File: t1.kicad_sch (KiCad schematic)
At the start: 47 parts, among them J1 Barrel_Jack_Switch, J2 USB_B, J3 P1, J4 2x2M, J5 ICSP1, J6 P2, U1 ATmega8U2-AU, Y1 16MHz

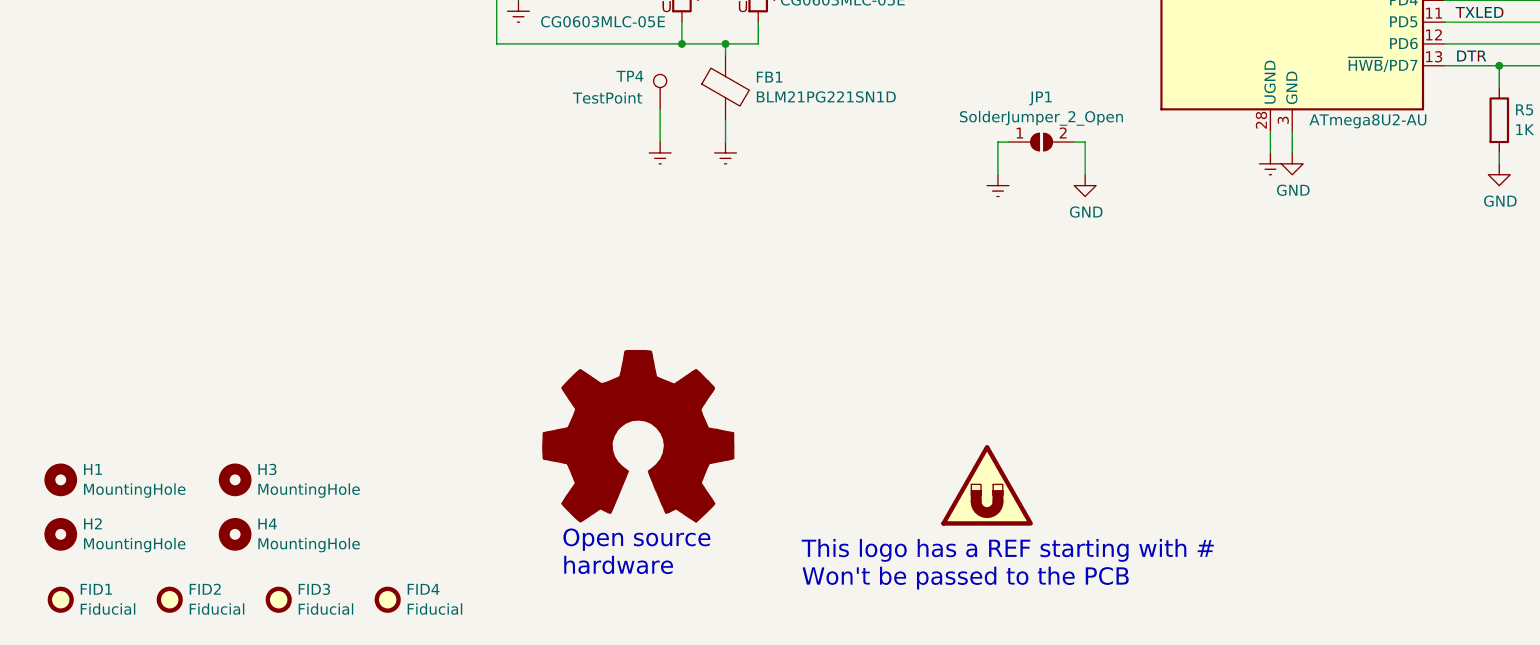
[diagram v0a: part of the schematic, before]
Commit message: More coherence between schematic and PCB
- Same time format, using the generation time stamp
- Same title, adding the variant
- Same worksheet. Why KiCad 6 doesn't respect the first page in the PCB?
- Same revision, short git hash
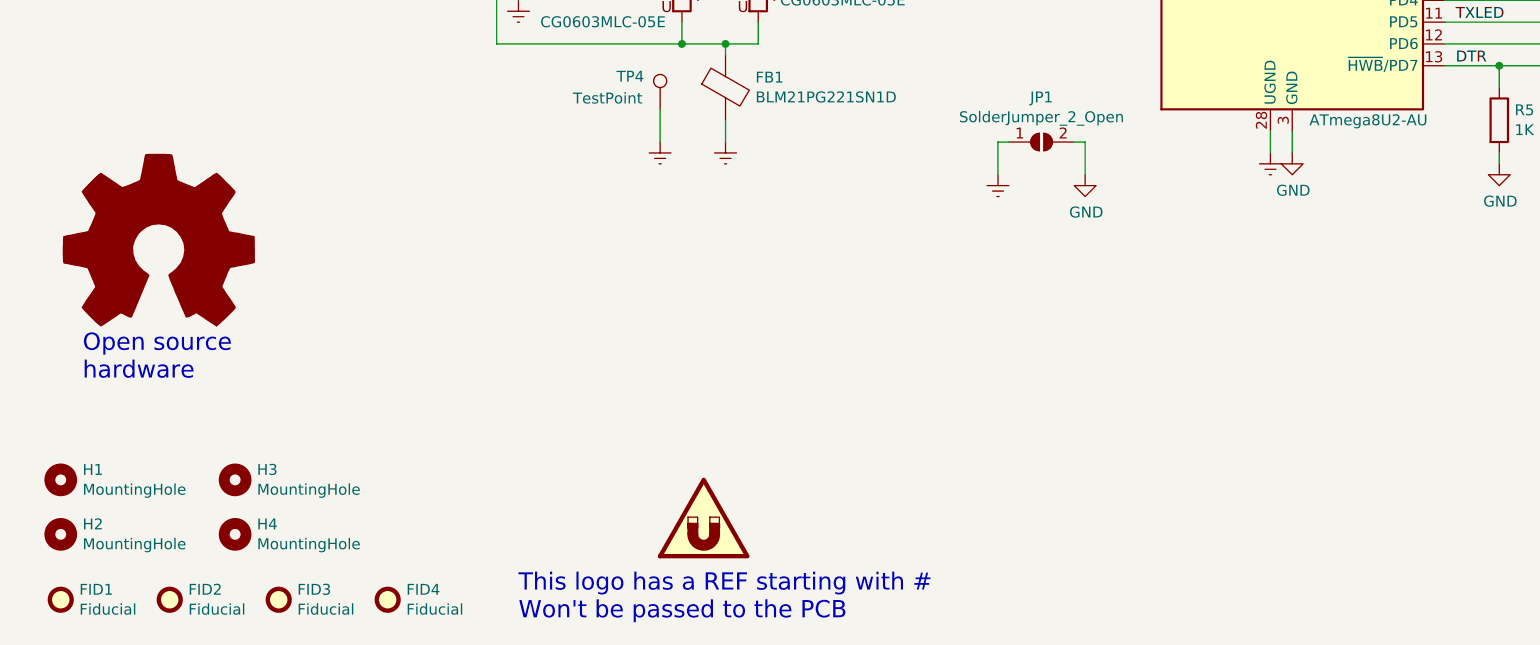
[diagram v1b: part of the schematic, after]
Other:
- company: Arduino -> Instituto Nacional de Tecnología Industrial
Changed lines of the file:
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@@
   (title_block
     (title "Arduino UNO programmer")
-    (date "2020-09-09")
-    (rev "r1")
-    (company "Arduino")
+    (date "${date}")
+    (rev "${git_hash}")
+    (company "Instituto Nacional de Tecnología Industrial")
     (comment 1 "Just a copy of the original circuit, but not as ugly")
+    (comment 4 "An example of KiBot variants")
   )
   (junction (at 82.55 88.9) (diameter 0) (color 0 0 0 0)
@@
     (stroke (width 0) (type default) (color 0 0 0 0))
   )
-  (text "Open source\nhardware" (at 77.47 187.96 0)
+  (text "Open source\nhardware" (at 21.59 165.1 0)
     (effects (font (size 2.0066 2.0066)) (justify left bottom))
   )
   (text "This logo has a REF starting with #\nWon't be passed to the PCB"
-    (at 105.41 189.23 0)
+    (at 72.39 193.04 0)
     (effects (font (size 2.0066 2.0066)) (justify left bottom))
   )
@@
     (pin "1")
   )
-  (symbol (lib_id "Graphic:SYM_Magnet_Large") (at 127 176.53 0) (unit 1)
-    (in_bom yes) (on_board yes)
-    (property "Reference" "#SYM1" (id 0) (at 127 171.45 0)
-      (effects (font (size 1.27 1.27)) hide)
-    )
-    (property "Value" "SYM_Magnet_Large" (id 1) (at 127 182.88 0)
-      (effects (font (size 1.27 1.27)) hide)
-    )
-    (property "Footprint" "" (id 2) (at 127 181.61 0)
-      (effects (font (size 1.27 1.27)) hide)
-    )
-    (property "Datasheet" "~" (id 3) (at 127.762 181.61 0)
+  (symbol (lib_id "Graphic:SYM_Magnet_Large") (at 93.98 180.34 0) (unit 1)
+    (in_bom yes) (on_board yes)
+    (property "Reference" "#SYM1" (id 0) (at 93.98 175.26 0)
+      (effects (font (size 1.27 1.27)) hide)
+    )
+    (property "Value" "SYM_Magnet_Large" (id 1) (at 93.98 186.69 0)
+      (effects (font (size 1.27 1.27)) hide)
+    )
+    (property "Footprint" "" (id 2) (at 93.98 185.42 0)
+      (effects (font (size 1.27 1.27)) hide)
+    )
+    (property "Datasheet" "~" (id 3) (at 94.742 185.42 0)
       (effects (font (size 1.27 1.27)) hide)
     )
@@
     )
   )
-  (symbol (lib_id "Graphic:Logo_Open_Hardware_Large") (at 86.36 172.72 0) (unit 1)
-    (in_bom yes) (on_board yes)
-    (property "Reference" "LOGO1" (id 0) (at 86.36 160.02 0)
-      (effects (font (size 1.27 1.27)) hide)
-    )
-    (property "Value" "Logo_Open_Hardware_Large" (id 1) (at 86.36 182.88 0)
-      (effects (font (size 1.27 1.27)) hide)
-    )
-    (property "Footprint" "Symbol:OSHW-Logo_11.4x12mm_SilkScreen" (id 2) (at 86.36 172.72 0)
-      (effects (font (size 1.27 1.27)) hide)
-    )
-    (property "Datasheet" "~" (id 3) (at 86.36 172.72 0)
-      (effects (font (size 1.27 1.27)) hide)
-    )
+  (symbol (lib_id "Graphic:Logo_Open_Hardware_Large") (at 30.48 149.86 0) (unit 1)
+    (in_bom yes) (on_board yes)
+    (property "Reference" "LOGO1" (id 0) (at 30.48 137.16 0)
+      (effects (font (size 1.27 1.27)) hide)
+    )
+    (property "Value" "Logo_Open_Hardware_Large" (id 1) (at 30.48 160.02 0)
+      (effects (font (size 1.27 1.27)) hide)
+    )
+    (property "Footprint" "Symbol:OSHW-Logo_11.4x12mm_SilkScreen" (id 2) (at 30.48 149.86 0)
+      (effects (font (size 1.27 1.27)) hide)
+    )
+    (property "Datasheet" "~" (id 3) (at 30.48 149.86 0)
+      (effects (font (size 1.27 1.27)) hide)
+    )

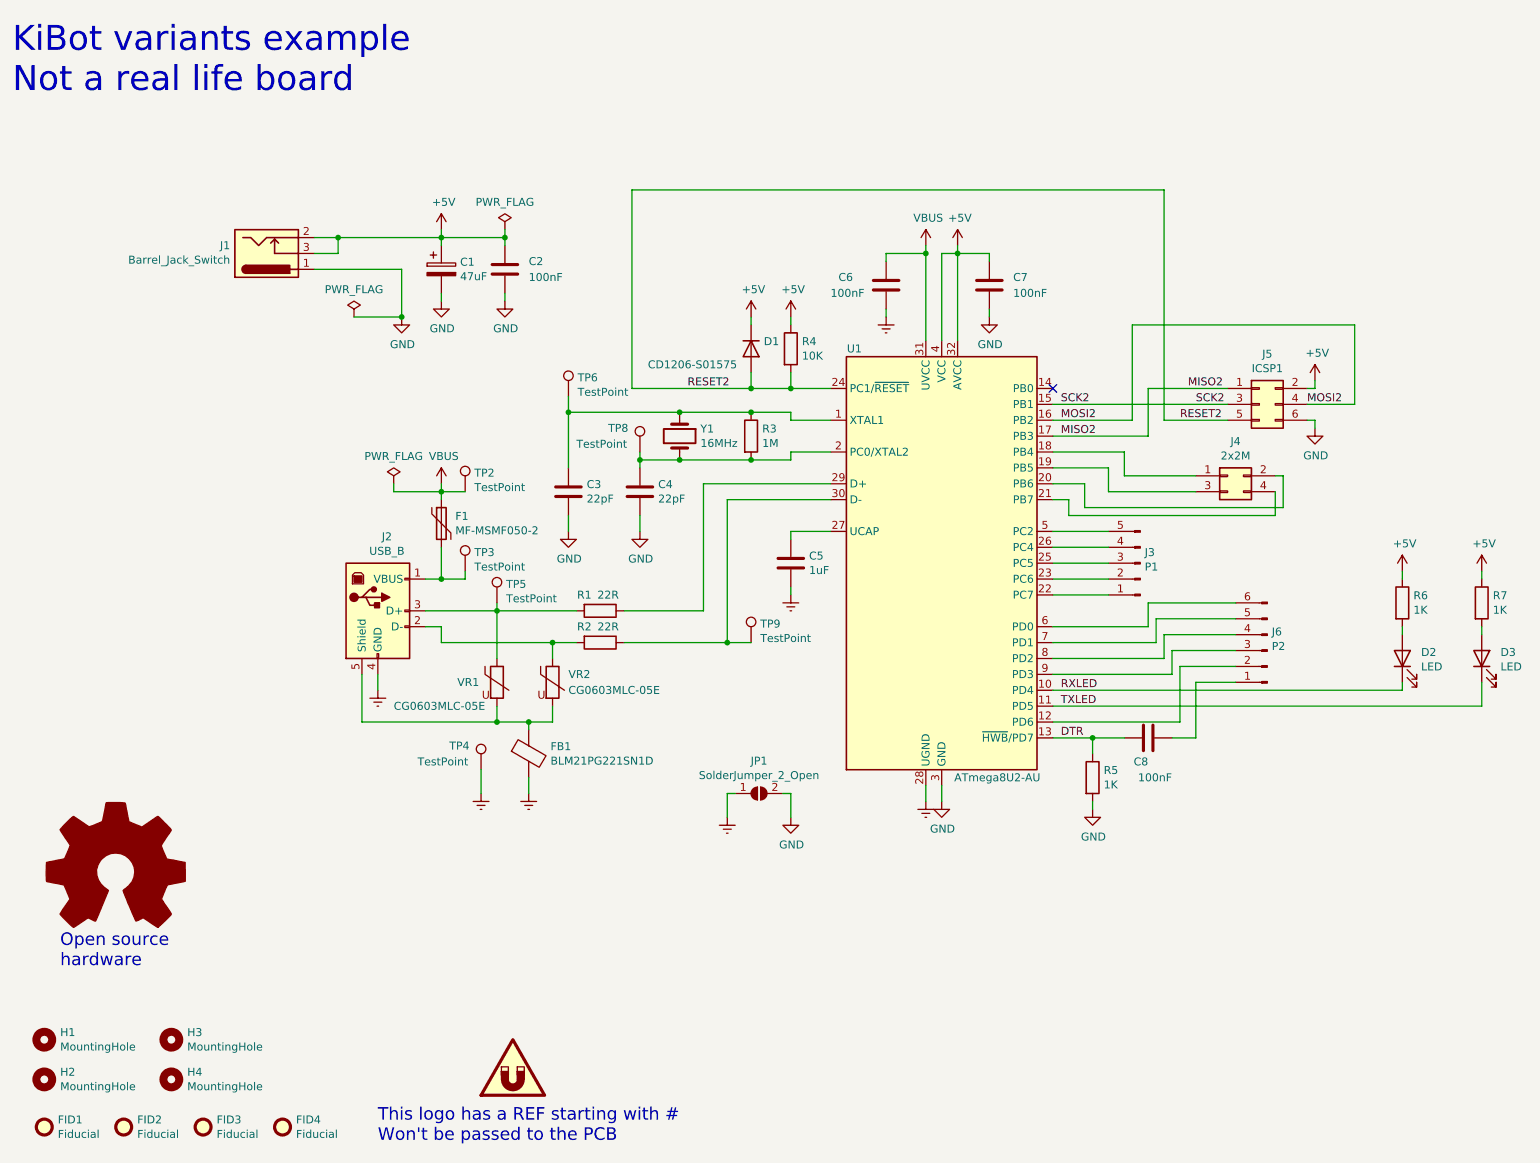
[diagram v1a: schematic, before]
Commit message: Migrated to KiCad 7
Also introduced some changes to get diffs
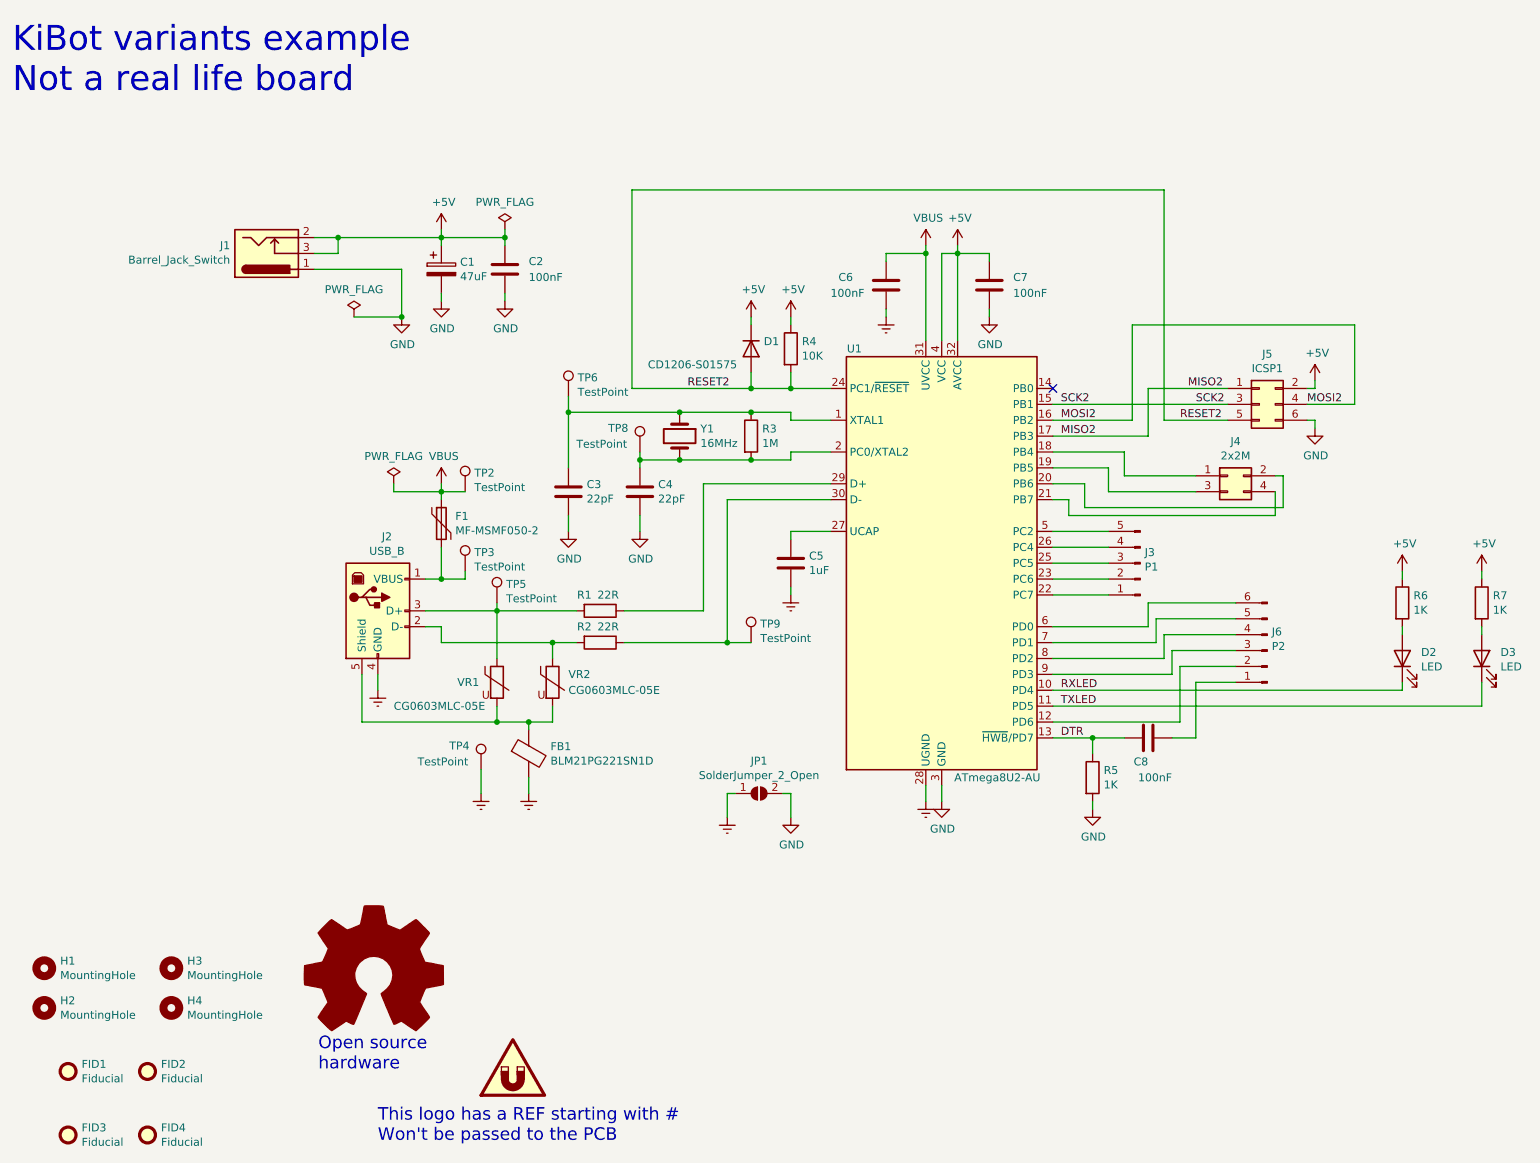
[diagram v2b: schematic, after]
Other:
- moved on the sheet: FID1, FID2, FID3, FID4, H1, H2, H3, H4
